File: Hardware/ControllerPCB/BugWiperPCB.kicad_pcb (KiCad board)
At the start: 4 copper layers, 110 x 40 mm, 110 parts, among them J1 UJ20-C-H-G-SMT-1-P16-TR, J2 1770924, J3 Phoenix_1776508, J4 RJ45, J5 Conn_TagConnect_TC2030-NL_ESP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, J6 1824420000, J7 Conn_01x02_Pin, J8 Micro_SD_Card, Q1 NMOS_SO-8, U1 ESP32-S3-WROOM-1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

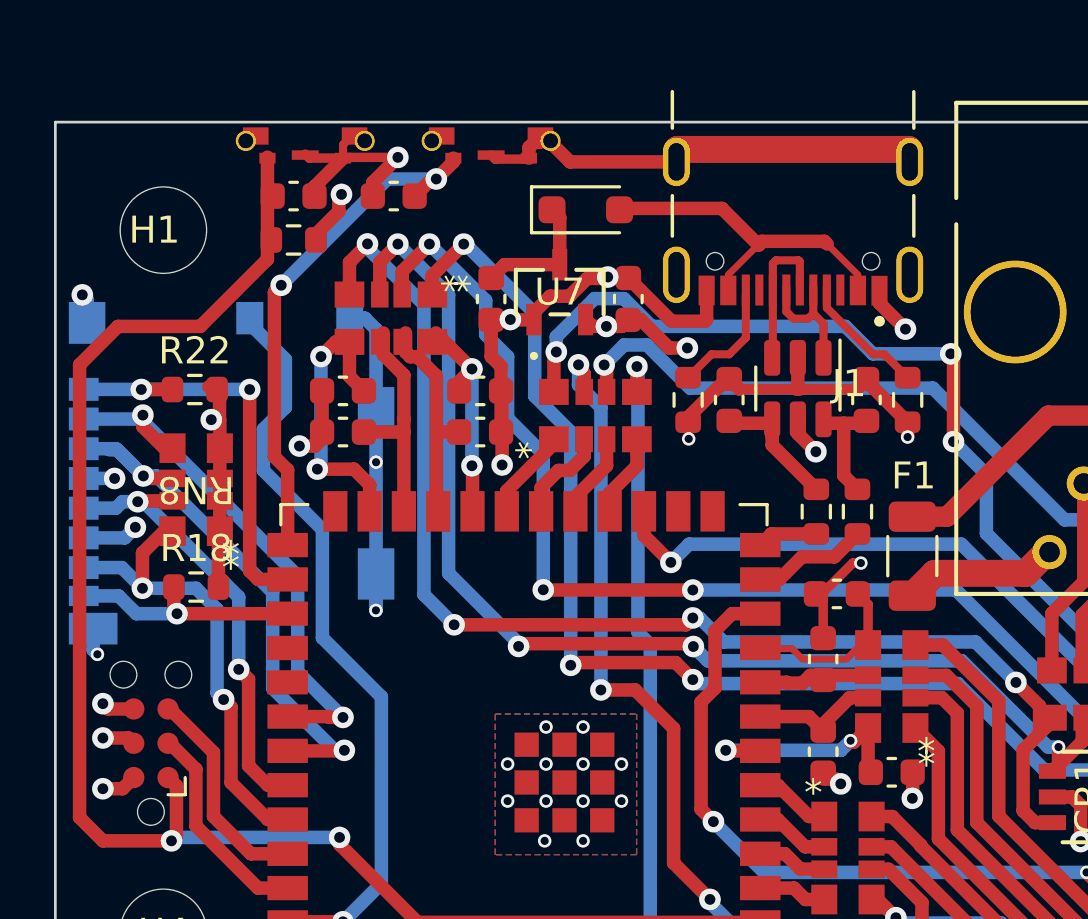
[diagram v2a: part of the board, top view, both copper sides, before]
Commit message: update USB-C Footprint
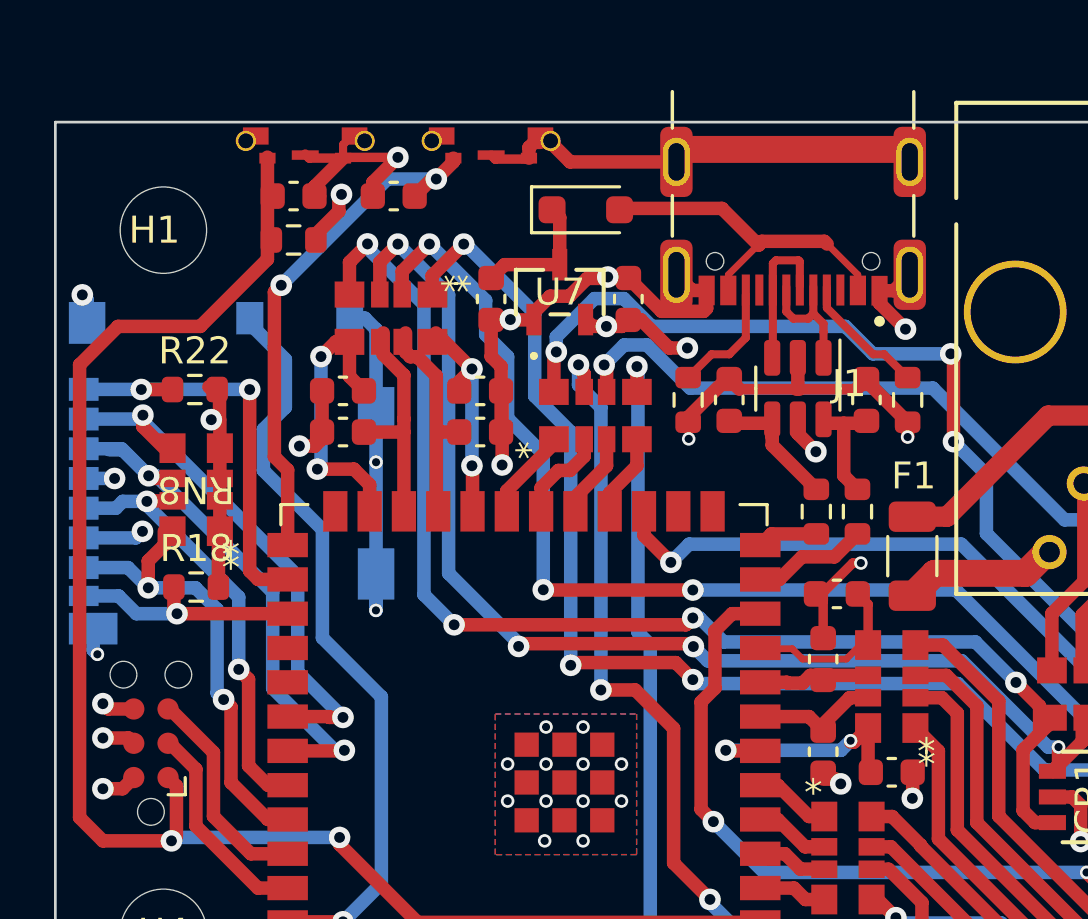
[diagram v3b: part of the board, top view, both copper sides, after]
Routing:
- net GND: track 133.8 -> 136.1 mm

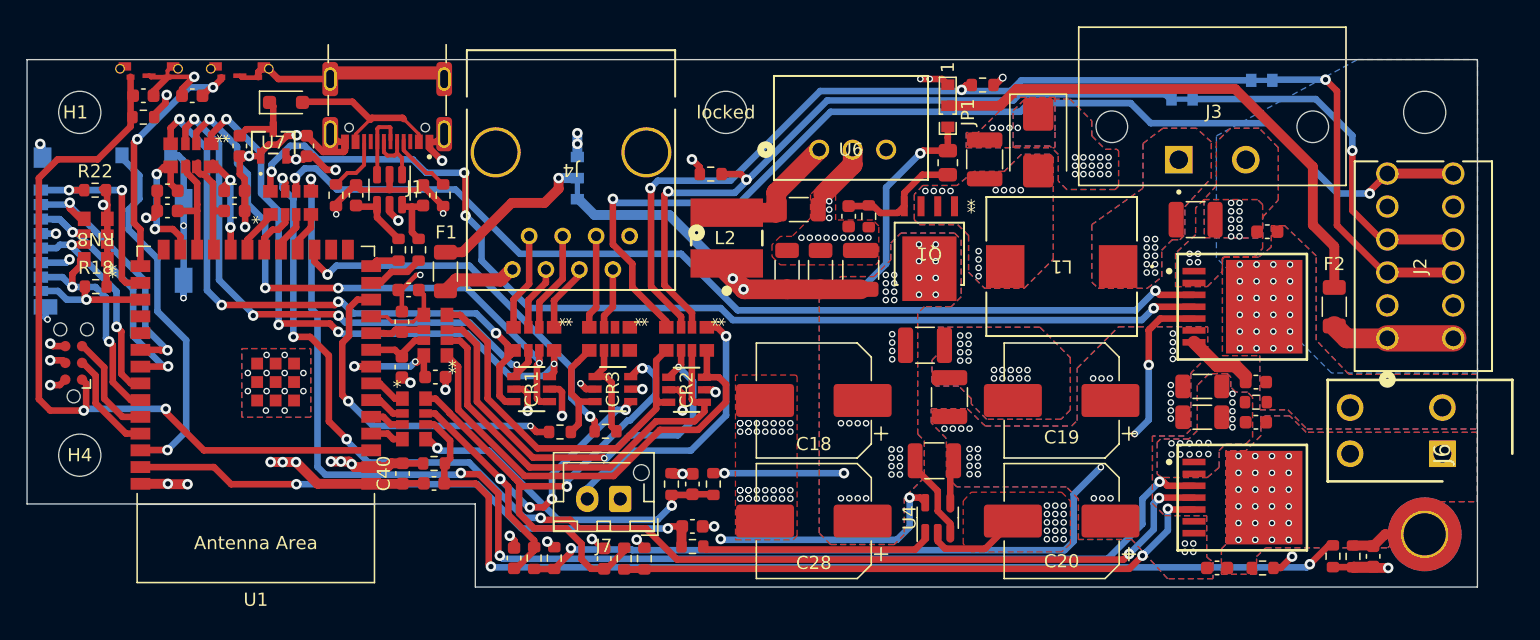
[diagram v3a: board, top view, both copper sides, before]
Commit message: update Controller PCB
Add Fuses for GND Signal Connectors, fix 3D and fix DRC
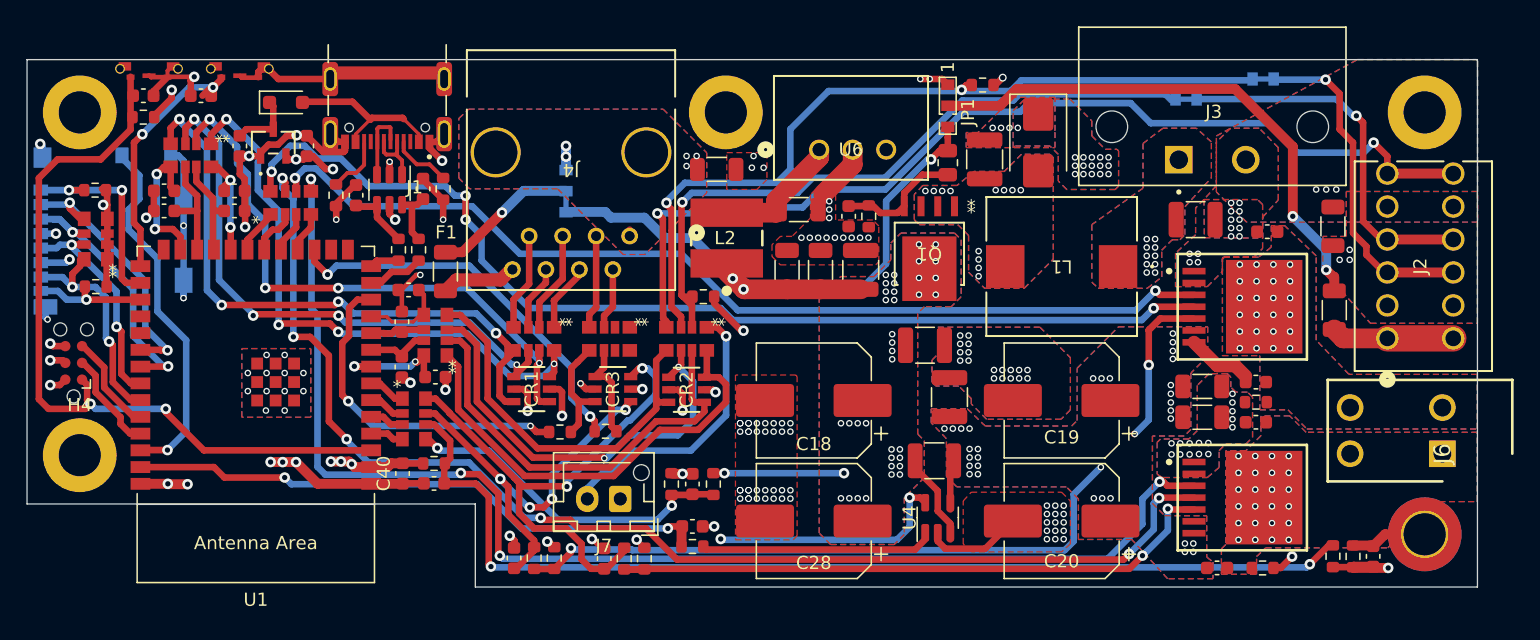
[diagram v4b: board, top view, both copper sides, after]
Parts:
- added F3: 100mA Polyfuse, Resistor_SMD:R_1206_3216Metric, F.Cu at (209.0, 72.6)
- added F4: 100mA Polyfuse, Resistor_SMD:R_1206_3216Metric, F.Cu at (162.3, 68.3)
- F2: value 10mA Polyfuse -> 100mA Polyfuse
- H1, H3, H4, locked: footprint MountingHole:MountingHole_3.2mm_M3_DIN965 -> MountingHole:MountingHole_3.2mm_M3_DIN965_Pad
- moved R17 9.31 mm to (161.3, 78.0), turned to 180 degrees
- moved JP4 1.31 mm to (150.9, 70.0)
- moved C3 0.66 mm to (123.2, 62.7)
- moved C2 0.49 mm to (140.0, 69.8)
- moved R2 0.49 mm to (141.6, 69.8)
- moved JP2 0.30 mm to (197.1, 63.0)
- moved F2 0.26 mm to (209.1, 79.0)
- moved C34 0.25 mm to (120.4, 71.5)
- moved C35 0.25 mm to (120.4, 70.0)
- moved JP3 0.14 mm to (202.9, 61.5)
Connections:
- J2 pad 10: GND -> /GND2
- J2 pad 3: GND -> /GND2
- J2 pad 4: GND -> /GND2
- J2 pad 9: GND -> /GND2
- J4 pad 1: GND -> /ESP32-S3/GND3
- J4 pad SH: GND -> /ESP32-S3/GND3
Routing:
- net sw_1: track 82.0 -> 76.4 mm
- net Enc_1: track 54.9 -> 51.4 mm, vias 2 -> 1
- net GND: track 136.1 -> 132.9 mm, vias 174 -> 181
- net Net-(JP4-C): track 12.9 -> 11.1 mm
- net /ESP32-S3/GND3: track 0.00 -> 1.00 mm, vias 0 -> 3
- net /ESP32-S3/M_INH2: track 81.6 -> 80.6 mm
- net EN_C1: track 27.5 -> 28.1 mm
- net Boot: track 42.2 -> 42.8 mm
- net Enc_2: track 61.3 -> 60.8 mm
- net Net-(JP1-C): vias 0 -> 2
- net /GND2: vias 0 -> 3
- added copper zone on B.Cu, net /ESP32-S3/GND3
- added copper zone on F.Cu, net /ESP32-S3/GND3
- added copper zone on B.Cu, net /GND2
- added copper zone on F.Cu, net /GND2
- added copper zone on In2.Cu, net /GND2

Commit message: export Gerber, edit text
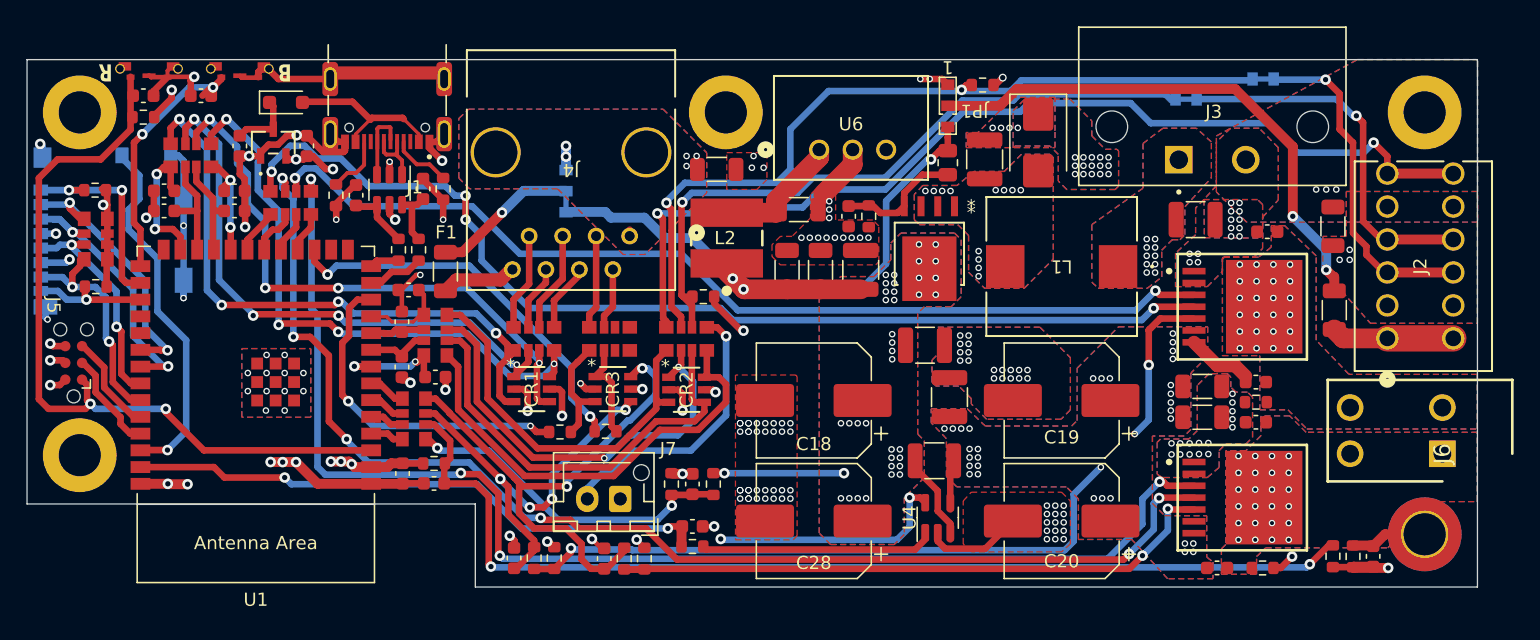
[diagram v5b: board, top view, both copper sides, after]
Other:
- board text added: "+12V | GND"
- board text added: "+V|IN3|IN1|OUT1 IN4|IN2|OUT2|GND"
- board text added: "B"
- board text added: "Boot"
- board text added: "BugWiper 2.0 Controller PCB Scholli"
- board text added: "Control Panel"
- board text added: "Encoder"
- board text added: "Motor"
- board text added: "Power Input"
- board text added: "R"
- board text added: "Reset"
- board text added: "S1|G|E1|E2|G|+V"
- board text added: "Shield"
- board text added: "TAG-Connect ESP-Prog Program"

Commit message: Update PCB
Add solder jumper for +3.3V selection
fix DRC
aligne vias
export Gerber
add text
fix 3D Models
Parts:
- added JP5: SolderJumper_2_Open, Jumper:SolderJumper-2_P1.3mm_Open_TrianglePad1.0x1.5mm, B.Cu at (137.4, 63.7)
- added JP6: SolderJumper_2_Open, Jumper:SolderJumper-2_P1.3mm_Open_TrianglePad1.0x1.5mm, B.Cu at (175.3, 63.2)
- J7: footprint Connector_JST:JST_XH_B2B-XH-AM_1x02_P2.50mm_Vertical -> BugWiper_lib:JST_XH_B2B-XH-AM_1x02_P2.50mm_Vertical
- moved CR3 0.29 mm to (154.1, 85.0)
- moved CR2 0.05 mm to (160.0, 85.0)
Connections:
- C29 pad 1: +3.3V -> /ESP32-S3/+3,3V
- U6 pad 3: +3.3V -> /Power/3V3
- U7 pad 2: +3.3V -> /ESP32-S3/+3,3V
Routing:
- net /ESP32-S3/+3,3V: track 0.00 -> 5.40 mm, vias 0 -> 2
- net +3.3V: track 52.4 -> 49.3 mm, vias 19 -> 26
- net Enc_2: track 60.8 -> 59.1 mm
- net Net-(U3-IS): track 65.5 -> 64.3 mm
- net GND: track 132.9 -> 131.7 mm, vias 181 -> 173
- net MOSI: track 20.9 -> 19.8 mm
- net sw_1: track 76.4 -> 77.1 mm, vias 2 -> 4
- net Enc_1: track 51.4 -> 52.0 mm
- net Net-(CR1-IO_4): track 44.9 -> 45.5 mm
- net /Power/3V3: vias 0 -> 3
- net /Power/+VBat: vias 10 -> 8
- net +12V_HighSide: vias 31 -> 30
- added copper zone on B.Cu, net +3.3V
- added copper zone on B.Cu, net /ESP32-S3/+3,3V
- added copper zone on B.Cu, net /Power/3V3
- added copper zone on F.Cu, net /Power/3V3
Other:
- board text added: "Power +12V"
- board text added: "Power USB"

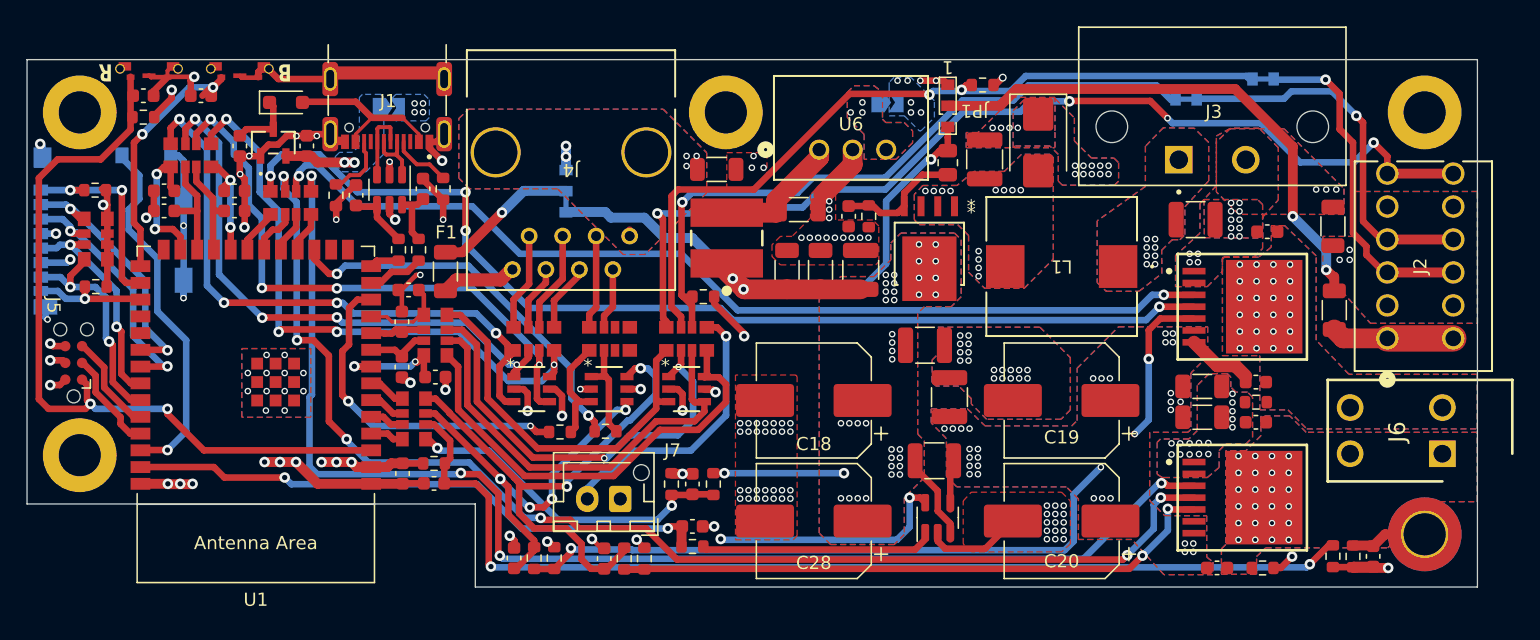
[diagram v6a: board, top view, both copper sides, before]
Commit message: update Controller PCB
Add additional capacitor
fix footprint Resistor Array CAT16
fix 3D Model CAT16
change traces from 0.5 to 0.4 mm
fix USB-C Footprint
Export Gerber
update BOM and Values
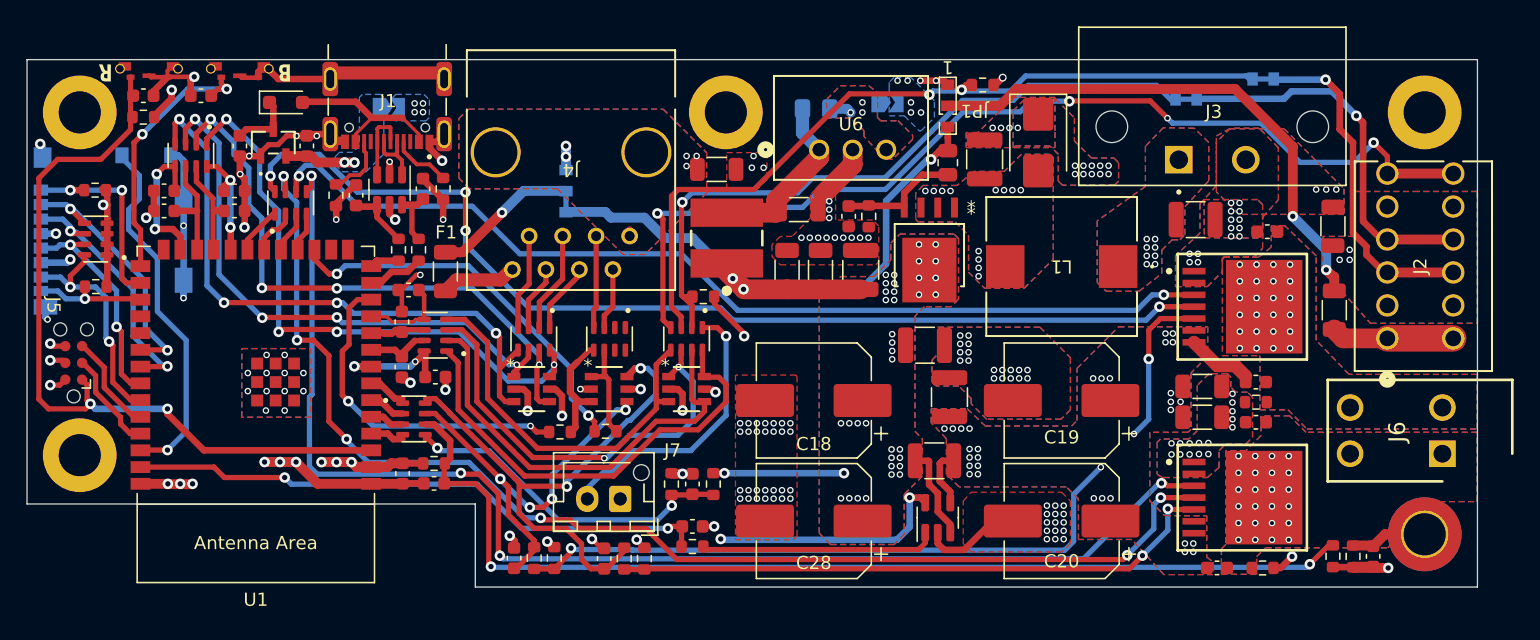
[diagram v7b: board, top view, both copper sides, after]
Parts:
- added C41: 1nF, Capacitor_SMD:C_0805_2012Metric_Pad1.18x1.45mm_HandSolder, B.Cu at (169.8, 63.7)
- Q1: value NMOS_SO-8 -> SQJ146ELP-T1_GE3
- RN1, RN2, RN5: value 1k_Pack04 -> 1k x 4; footprint BugWiper_lib:BO_CAY16 -> BugWiper_lib:RESCAV80P320X155X60-8N
- RN3, RN6, RN7: value 100R_Pack04 -> 100R x 4; footprint BugWiper_lib:BO_CAY16 -> BugWiper_lib:RESCAV80P320X155X60-8N
- RN4: value 2k2_Pack04 -> 10k x 4; footprint BugWiper_lib:BO_CAY16 -> BugWiper_lib:RESCAV80P320X155X60-8N
- RN8: value 1k_Pack04 -> 10k x 4; footprint BugWiper_lib:BO_CAY16 -> BugWiper_lib:RESCAV80P320X155X60-8N
- moved Q1 0.10 mm to (178.4, 74.8)
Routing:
- net Net-(U6-+VIN): track 9.88 -> 13.5 mm
- net /Power/3V3: track 0.00 -> 1.69 mm
- net Boot: track 42.8 -> 44.1 mm
- net GND: track 131.7 -> 132.4 mm
- net /ESP32-S3/ADC_INA: track 17.2 -> 17.9 mm
- net +12V_HighSide: track 9.22 -> 9.88 mm

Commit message: update BOM
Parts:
- removed U5: WE-TVS-82400102, Package_TO_SOT_SMD:SOT-23-6
- added CR4: D5V0P4UR6SO-7, BugWiper_lib:SOT26_DIO, F.Cu at (137.5, 70.0)
- C10, C7: value 100uF -> 22uF 25V
- C14, C32, C33, C34, C35, C36, C37: value 10nF -> 10nF
- C15, C16, C17, C21, C23: value 25uF -> 22uF 25V
- C18, C19, C20, C28: value 470uF -> 470uF 16V
- C22, C27, C29, C3, C30, C31, C38, C39: value 100nF -> 100nF
- C24, C25, C26: value 4.7uF -> 22uF 25V
- C4: value 1uF -> 100nF
- C40: value 1uF -> 1uF 50V; footprint Capacitor_SMD:C_0603_1608Metric -> Capacitor_SMD:C_0805_2012Metric
- C5, C9: value 100nF -> 1uF 50V; footprint Capacitor_SMD:C_0603_1608Metric -> Capacitor_SMD:C_0805_2012Metric
- D2: value D_Zener -> D_Zener 10V; footprint Resistor_SMD:R_0805_2012Metric -> Diode_SMD:D_SOD-323_HandSoldering
- D3: value D_TVS -> D_TVS 15V
- R10, R11: value 4k7 -> 10k
- moved C31 0.63 mm to (141.5, 92.1)
- moved R38 0.63 mm to (141.5, 90.6)
- moved C5 0.39 mm to (203.5, 87.8)
- moved C40 0.27 mm to (138.8, 91.4)
- moved JP1 0.25 mm to (179.8, 63.2)
- moved C9 0.19 mm to (204.2, 73.1)
- moved D2 0.07 mm to (179.8, 67.8)
- moved C8 0.05 mm to (203.2, 84.5)
- moved R8 0.05 mm to (203.2, 86.0)
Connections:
- C1 pad 2: Net-(C1-Pad2) -> Net-(CR4-IO_2)
- C2 pad 1: Net-(C2-Pad1) -> Net-(CR4-IO_1)
- J1 pad A6: Net-(J1-DP1) -> Net-(CR4-IO_2)
- J1 pad A7: Net-(J1-DN1) -> Net-(CR4-IO_1)
- J1 pad B6: Net-(J1-DP1) -> Net-(CR4-IO_2)
- J1 pad B7: Net-(J1-DN1) -> Net-(CR4-IO_1)
- R4 pad 1: Net-(C1-Pad2) -> Net-(CR4-IO_2)
- R5 pad 1: Net-(C2-Pad1) -> Net-(CR4-IO_1)
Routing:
- net Net-(CR4-IO_2): track 0.00 -> 14.3 mm
- net Net-(CR4-IO_1): track 0.00 -> 12.5 mm
- net Net-(C1-Pad2): track 5.58 -> 0.00 mm
- net Net-(J1-DP1): track 5.50 -> 0.00 mm
- net Net-(J1-DN1): track 4.84 -> 0.00 mm
- net Net-(C2-Pad1): track 4.43 -> 0.00 mm
- net GND: track 132.4 -> 133.3 mm
- net /ESP32-S3/ADC_NTC: track 79.6 -> 78.8 mm
- net +3.3V: track 49.3 -> 50.0 mm
